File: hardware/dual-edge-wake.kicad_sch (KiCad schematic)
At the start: 17 parts, among them J1 Conn_01x04_Male, J2 Circuit, J3 Falling, J4 Leading, Q1 BC807, Q2 BC847, Q3 BC847, U1 SN74LVC1G86DBVR

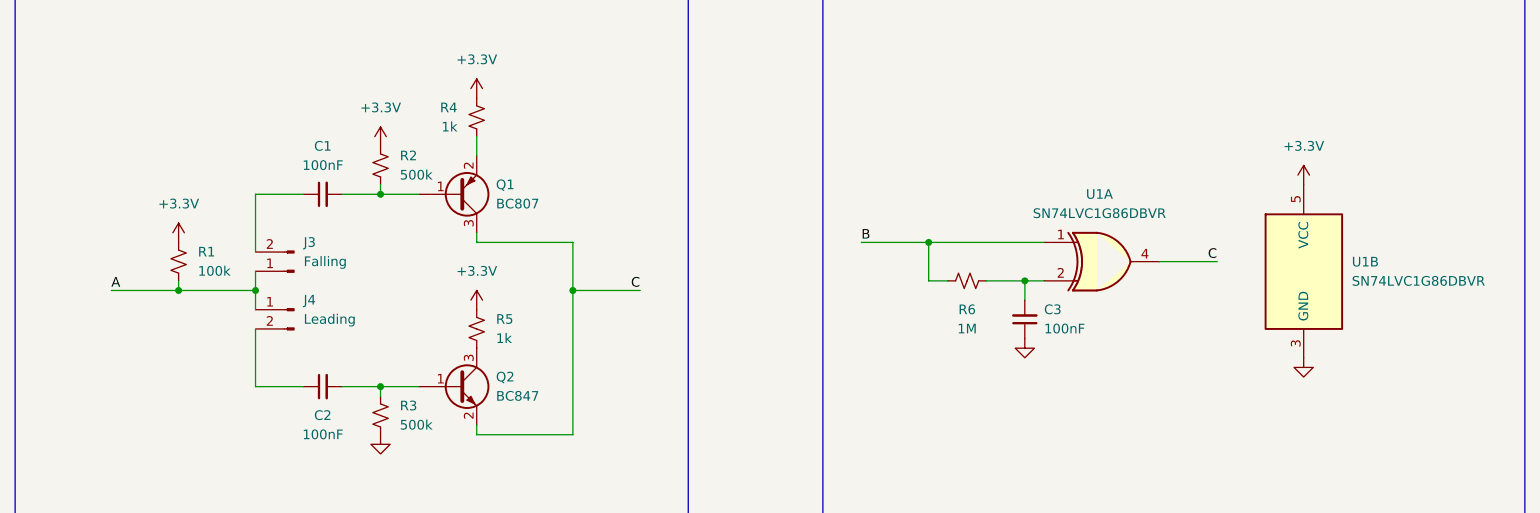
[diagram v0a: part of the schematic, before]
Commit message: Fixed #2
Add resistor between circuit outputs, removed pull-up on circuit A input. Also add rear SS
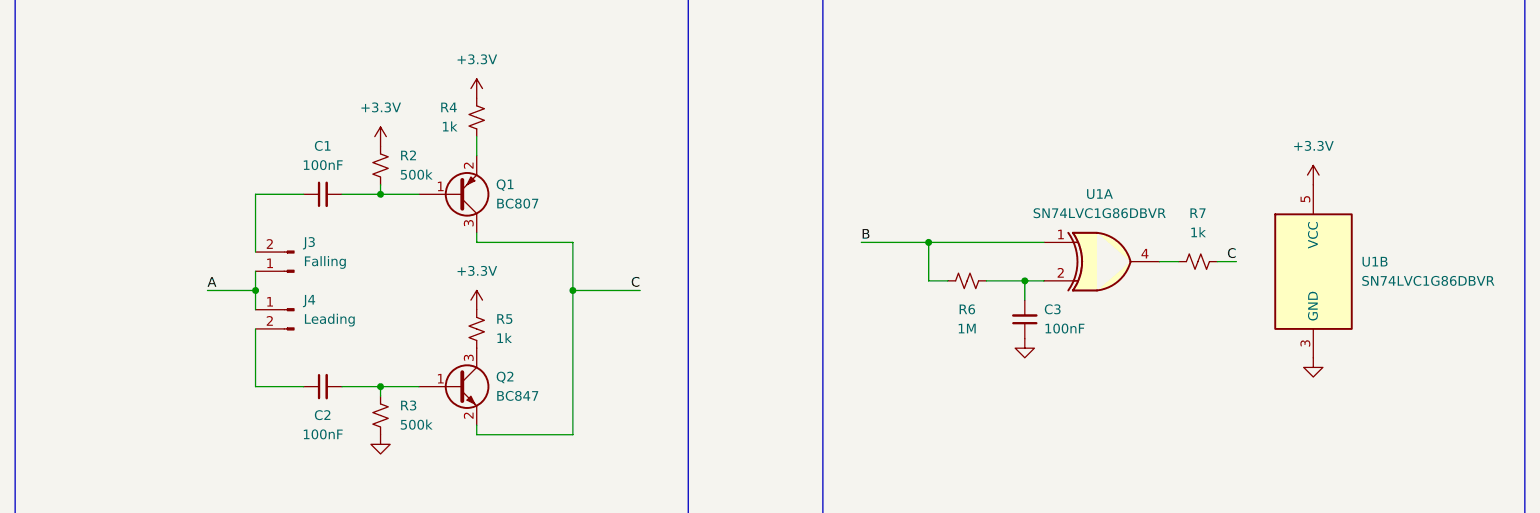
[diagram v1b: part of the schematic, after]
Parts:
- removed R1: 100k, Resistor_SMD:R_0805_2012Metric_Pad1.20x1.40mm_HandSolder, symbol Device:R_Small_US
- added R7: 1k, Resistor_SMD:R_0805_2012Metric_Pad1.20x1.40mm_HandSolder, symbol Device:R_Small_US
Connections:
- net C: now also R7.2; no longer U1.4
- new net: R7.1, U1.4
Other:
- moved on the sheet: U1B
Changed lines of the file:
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@@
   (junction (at 171.45 110.49) (diameter 0) (color 0 0 0 0)
   )
-  (junction (at 72.39 116.84) (diameter 0) (color 0 0 0 0)
-  )
   (junction (at 124.46 116.84) (diameter 0) (color 0 0 0 0)
   )
@@
     (stroke (width 0) (type default) (color 0 0 0 0))
   )
+  (wire (pts (xy 209.55 113.03) (xy 212.09 113.03))
+    (stroke (width 0) (type default) (color 0 0 0 0))
+  )
   (wire (pts (xy 99.06 44.45) (xy 111.76 44.45))
     (stroke (width 0) (type default) (color 0 0 0 0))
@@
     (stroke (width 0) (type default) (color 0 0 0 0))
   )
-  (wire (pts (xy 63.5 116.84) (xy 72.39 116.84))
-    (stroke (width 0) (type default) (color 0 0 0 0))
-  )
   (wire (pts (xy 148.59 45.72) (xy 156.21 45.72))
     (stroke (width 0) (type default) (color 0 0 0 0))
@@
     (stroke (width 0) (type default) (color 0 0 0 0))
   )
-  (wire (pts (xy 201.93 113.03) (xy 209.55 113.03))
-    (stroke (width 0) (type default) (color 0 0 0 0))
-  )
   (wire (pts (xy 82.55 111.76) (xy 82.55 104.14))
     (stroke (width 0) (type default) (color 0 0 0 0))
@@
     (stroke (width 0) (type default) (color 0 0 0 0))
   )
+  (wire (pts (xy 204.47 113.03) (xy 201.93 113.03))
+    (stroke (width 0) (type default) (color 0 0 0 0))
+  )
   (wire (pts (xy 196.85 38.1) (xy 190.5 38.1))
     (stroke (width 0) (type default) (color 0 0 0 0))
@@
     (stroke (width 0) (type default) (color 0 0 0 0))
   )
-  (wire (pts (xy 72.39 116.84) (xy 82.55 116.84))
+  (wire (pts (xy 76.2 116.84) (xy 82.55 116.84))
     (stroke (width 0) (type default) (color 0 0 0 0))
   )
@@
   )
   (wire (pts (xy 124.46 116.84) (xy 124.46 135.89))
-    (stroke (width 0) (type default) (color 0 0 0 0))
-  )
-  (wire (pts (xy 72.39 115.57) (xy 72.39 116.84))
     (stroke (width 0) (type default) (color 0 0 0 0))
   )
@@
     (effects (font (size 1.27 1.27)) (justify right bottom))
   )
-  (label "A" (at 63.5 116.84 0)
+  (label "A" (at 76.2 116.84 0)
     (effects (font (size 1.27 1.27)) (justify left bottom))
   )
@@
     (effects (font (size 1.27 1.27)) (justify right bottom))
   )
-  (label "C" (at 209.55 113.03 180)
+  (label "C" (at 212.09 113.03 180)
     (effects (font (size 1.27 1.27)) (justify right bottom))
   )
@@
     (effects (font (size 1.27 1.27)) (justify left bottom))
   )
-  (symbol (lib_id "power:GND") (at 220.98 125.73 0) (mirror y) (unit 1)
-    (in_bom yes) (on_board yes) (fields_autoplaced)
-    (property "Reference" "#PWR09" (id 0) (at 220.98 132.08 0)
-      (effects (font (size 1.27 1.27)) hide)
-    )
-    (property "Value" "GND" (id 1) (at 220.98 130.81 0)
-      (effects (font (size 1.27 1.27)) hide)
-    )
-    (property "Footprint" "" (id 2) (at 220.98 125.73 0)
-      (effects (font (size 1.27 1.27)) hide)
-    )
-    (property "Datasheet" "" (id 3) (at 220.98 125.73 0)
+  (symbol (lib_id "power:GND") (at 222.25 125.73 0) (mirror y) (unit 1)
+    (in_bom yes) (on_board yes) (fields_autoplaced)
+    (property "Reference" "#PWR09" (id 0) (at 222.25 132.08 0)
+      (effects (font (size 1.27 1.27)) hide)
+    )
+    (property "Value" "GND" (id 1) (at 222.25 130.81 0)
+      (effects (font (size 1.27 1.27)) hide)
+    )
+    (property "Footprint" "" (id 2) (at 222.25 125.73 0)
+      (effects (font (size 1.27 1.27)) hide)
+    )
+    (property "Datasheet" "" (id 3) (at 222.25 125.73 0)
       (effects (font (size 1.27 1.27)) hide)
     )
@@
     )
     (property "Datasheet" "" (id 3) (at 99.06 135.89 0)
-      (effects (font (size 1.27 1.27)) hide)
-    )
-    (pin "1")
-  )
-  (symbol (lib_id "power:+3.3V") (at 72.39 110.49 0) (unit 1)
-    (in_bom yes) (on_board yes) (fields_autoplaced)
-    (property "Reference" "#PWR01" (id 0) (at 72.39 114.3 0)
-      (effects (font (size 1.27 1.27)) hide)
-    )
-    (property "Value" "+3.3V" (id 1) (at 72.39 105.41 0))
-    (property "Footprint" "" (id 2) (at 72.39 110.49 0)
-      (effects (font (size 1.27 1.27)) hide)
-    )
-    (property "Datasheet" "" (id 3) (at 72.39 110.49 0)
       (effects (font (size 1.27 1.27)) hide)
     )
@@
     (pin "3")
   )
-  (symbol (lib_id "Nick:SN74LVC1G86DBVR") (at 220.98 102.87 0) (unit 2)
-    (in_bom yes) (on_board yes) (fields_autoplaced)
-    (property "Reference" "U1" (id 0) (at 227.33 113.0807 0)
-      (effects (font (size 1.27 1.27)) (justify left))
-    )
-    (property "Value" "SN74LVC1G86DBVR" (id 1) (at 227.33 115.6207 0)
-      (effects (font (size 1.27 1.27)) (justify left))
-    )
-    (property "Footprint" "Package_TO_SOT_SMD:SOT-23-5_HandSoldering" (id 2) (at 222.5548 93.472 0)
-      (effects (font (size 1.27 1.27)) hide)
-    )
-    (property "Datasheet" "https://datasheet.lcsc.com/lcsc/1912111437_Texas-Instruments-SN74LVC1G86DBVR_C402161.pdf" (id 3) (at 222.504 96.012 0)
-      (effects (font (size 1.27 1.27)) hide)
-    )
-    (property "LCSC" "C402161" (id 4) (at 222.504 98.298 0)
+  (symbol (lib_id "Nick:SN74LVC1G86DBVR") (at 222.25 102.87 0) (unit 2)
+    (in_bom yes) (on_board yes) (fields_autoplaced)
+    (property "Reference" "U1" (id 0) (at 228.6 113.0807 0)
+      (effects (font (size 1.27 1.27)) (justify left))
+    )
+    (property "Value" "SN74LVC1G86DBVR" (id 1) (at 228.6 115.6207 0)
+      (effects (font (size 1.27 1.27)) (justify left))
+    )
+    (property "Footprint" "Package_TO_SOT_SMD:SOT-23-5_HandSoldering" (id 2) (at 223.8248 93.472 0)
+      (effects (font (size 1.27 1.27)) hide)
+    )
+    (property "Datasheet" "https://datasheet.lcsc.com/lcsc/1912111437_Texas-Instruments-SN74LVC1G86DBVR_C402161.pdf" (id 3) (at 223.774 96.012 0)
+      (effects (font (size 1.27 1.27)) hide)
+    )
+    (property "LCSC" "C402161" (id 4) (at 223.774 98.298 0)
       (effects (font (size 1.27 1.27)) hide)
     )
@@
     (pin "1")
   )
-  (symbol (lib_id "Device:R_Small_US") (at 72.39 113.03 0) (unit 1)
-    (in_bom yes) (on_board yes)
-    (property "Reference" "R1" (id 0) (at 74.93 111.7599 0)
-      (effects (font (size 1.27 1.27)) (justify left))
-    )
-    (property "Value" "100k" (id 1) (at 74.93 114.2999 0)
-      (effects (font (size 1.27 1.27)) (justify left))
-    )
-    (property "Footprint" "Resistor_SMD:R_0805_2012Metric_Pad1.20x1.40mm_HandSolder" (id 2) (at 72.39 113.03 0)
-      (effects (font (size 1.27 1.27)) hide)
-    )
-    (property "Datasheet" "~" (id 3) (at 72.39 113.03 0)
-      (effects (font (size 1.27 1.27)) hide)
-    )
-    (property "LCSC" "C180850" (id 4) (at 72.39 113.03 0)
-      (effects (font (size 1.27 1.27)) hide)
-    )
-    (pin "1")
-    (pin "2")
-  )
   (symbol (lib_name "SN74LVC1G86DBVR_1") (lib_id "Nick:SN74LVC1G86DBVR") (at 186.5632 110.5408 0) (unit 1)
     (in_bom yes) (on_board yes) (fields_autoplaced)
@@
     (pin "2")
   )
-  (symbol (lib_id "power:+3.3V") (at 220.98 102.87 0) (unit 1)
-    (in_bom yes) (on_board yes) (fields_autoplaced)
-    (property "Reference" "#PWR08" (id 0) (at 220.98 106.68 0)
-      (effects (font (size 1.27 1.27)) hide)
-    )
-    (property "Value" "+3.3V" (id 1) (at 220.98 97.79 0))
-    (property "Footprint" "" (id 2) (at 220.98 102.87 0)
-      (effects (font (size 1.27 1.27)) hide)
-    )
-    (property "Datasheet" "" (id 3) (at 220.98 102.87 0)
-      (effects (font (size 1.27 1.27)) hide)
-    )
-    (pin "1")
+  (symbol (lib_id "power:+3.3V") (at 222.25 102.87 0) (unit 1)
+    (in_bom yes) (on_board yes) (fields_autoplaced)
+    (property "Reference" "#PWR08" (id 0) (at 222.25 106.68 0)
+      (effects (font (size 1.27 1.27)) hide)
+    )
+    (property "Value" "+3.3V" (id 1) (at 222.25 97.79 0))
+    (property "Footprint" "" (id 2) (at 222.25 102.87 0)
+      (effects (font (size 1.27 1.27)) hide)
+    )
+    (property "Datasheet" "" (id 3) (at 222.25 102.87 0)
+      (effects (font (size 1.27 1.27)) hide)
+    )
+    (pin "1")
+  )
+  (symbol (lib_id "Device:R_Small_US") (at 207.01 113.03 90) (unit 1)
+    (in_bom yes) (on_board yes) (fields_autoplaced)
+    (property "Reference" "R7" (id 0) (at 207.01 106.68 90))
+    (property "Value" "1k" (id 1) (at 207.01 109.22 90))
+    (property "Footprint" "Resistor_SMD:R_0805_2012Metric_Pad1.20x1.40mm_HandSolder" (id 2) (at 207.01 113.03 0)
+      (effects (font (size 1.27 1.27)) hide)
+    )
+    (property "Datasheet" "~" (id 3) (at 207.01 113.03 0)
+      (effects (font (size 1.27 1.27)) hide)
+    )
+    (property "LCSC" "C79496" (id 4) (at 207.01 113.03 0)
+      (effects (font (size 1.27 1.27)) hide)
+    )
+    (pin "1")
+    (pin "2")
   )
   (symbol (lib_id "Device:R_Small_US") (at 99.06 100.33 0) (unit 1)
@@
       (reference "#FLG0102") (unit 1) (value "PWR_FLAG") (footprint "")
     )
-    (path "/519bb034-8ec7-4580-b8a2-846d03477e01"
-      (reference "#PWR01") (unit 1) (value "+3.3V") (footprint "")
-    )
     (path "/b9fd35fa-a805-4834-b677-93fcf2815622"
       (reference "#PWR02") (unit 1) (value "+3.3V") (footprint "")
@@
       (reference "Q3") (unit 1) (value "BC847") (footprint "Package_TO_SOT_SMD:SOT-23_Handsoldering")
     )
-    (path "/730c3d3a-7dea-4bc9-944a-8fb9d40a96d9"
-      (reference "R1") (unit 1) (value "100k") (footprint "Resistor_SMD:R_0805_2012Metric_Pad1.20x1.40mm_HandSolder")
-    )
     (path "/f1700800-59a4-49ff-9258-d222d3e487dd"
       (reference "R2") (unit 1) (value "500k") (footprint "Resistor_SMD:R_0805_2012Metric_Pad1.20x1.40mm_HandSolder")
@@
       (reference "R6") (unit 1) (value "1M") (footprint "Resistor_SMD:R_0805_2012Metric_Pad1.20x1.40mm_HandSolder")
     )
+    (path "/eef367e8-9445-418c-8bc3-248e727c8ddd"
+      (reference "R7") (unit 1) (value "1k") (footprint "Resistor_SMD:R_0805_2012Metric_Pad1.20x1.40mm_HandSolder")
+    )
     (path "/80885ac7-b5dc-4c53-80ea-fe4770c448b7"

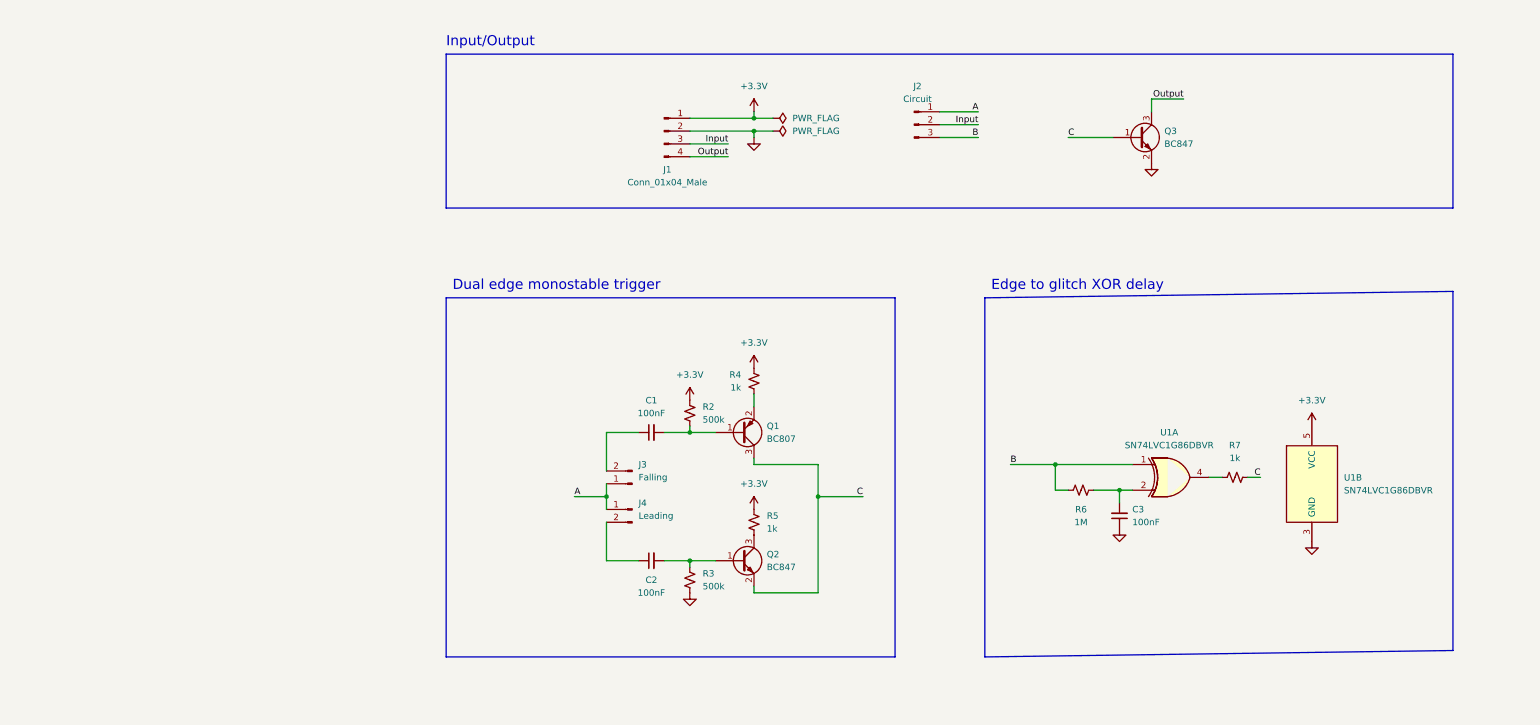
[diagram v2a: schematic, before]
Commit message: WIP - Add pull ups and LEDs
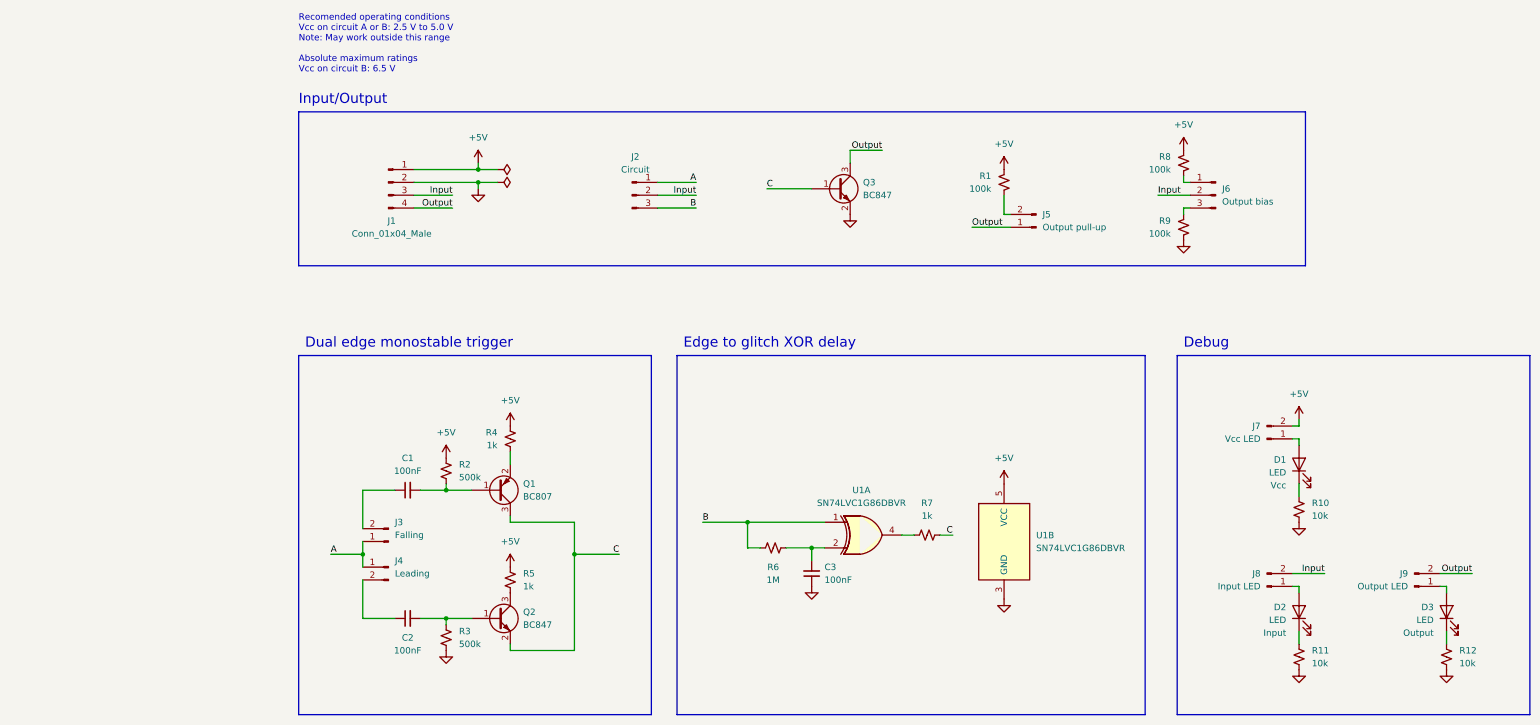
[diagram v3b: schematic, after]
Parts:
- added D1, D2, D3: LED, LED_SMD:LED_0603_1608Metric_Pad1.05x0.95mm_HandSolder, symbol Device:LED
- added J5: Output pull-up, Jumper:SolderJumper-2_P1.3mm_Open_RoundedPad1.0x1.5mm, symbol Connector:Conn_01x02_Male
- added J6: Output bias, Nick:SolderJumper-3_HL, symbol Connector:Conn_01x03_Male
- added J7: Vcc LED, Jumper:SolderJumper-2_P1.3mm_Open_RoundedPad1.0x1.5mm, symbol Connector:Conn_01x02_Male
- added J8: Input LED, Jumper:SolderJumper-2_P1.3mm_Open_RoundedPad1.0x1.5mm, symbol Connector:Conn_01x02_Male
- added J9: Output LED, Jumper:SolderJumper-2_P1.3mm_Open_RoundedPad1.0x1.5mm, symbol Connector:Conn_01x02_Male
- added R1, R8, R9: 100k, Resistor_SMD:R_0805_2012Metric_Pad1.20x1.40mm_HandSolder, symbol Device:R_Small_US
- added R10, R11, R12: 10k, Resistor_SMD:R_0805_2012Metric_Pad1.20x1.40mm_HandSolder, symbol Device:R_Small_US
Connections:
- net GND: now also R10.1, R11.1, R12.1, R9.1
- net Input: now also J6.2 (Pin_2), J8.2 (Pin_2)
- net Output: now also J5.1 (Pin_1), J9.2 (Pin_2)
- net +3.3V renamed +5V
- net +5V: now also J7.2 (Pin_2), R1.2, R8.2
- new net: J6.1 (Pin_1), R8.1
- new net: J6.3 (Pin_3), R9.2
- new net: D3.1 (K), R12.2
- new net: D2.1 (K), R11.2
- new net: D2.2 (A), J8.1 (Pin_1)
- new net: J5.2 (Pin_2), R1.1
- new net: D3.2 (A), J9.1 (Pin_1)
- new net: D1.2 (A), J7.1 (Pin_1)
- new net: D1.1 (K), R10.2
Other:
- note added: "Debug"
- note added: "Recomended operating conditions Vcc on circuit A or B: 2.5 V to 5.0 V Note: May work outside this range Absolute maximum ratings Vcc on circuit B: 6.5 V"
- moved on the sheet: C1, C2, C3, J1, J2, J3, J4, Q1, Q2, Q3, R2, R3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
